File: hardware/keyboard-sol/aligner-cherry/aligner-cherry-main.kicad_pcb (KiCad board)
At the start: 2 copper layers, 324 x 116.9 mm, 75 parts, among them SW10 TAB: 1.25x, SW11 I, SW12 2, SW13 Zero, SW14 Q, SW15 O, SW16 3, SW17 Dash, SW18 W, SW19 P, SW20 4, SW21 Caret, SW22 E, SW23 AT, SW24 5, SW25 LT Bracket, SW26 R, SW27 Return: 1.5x, SW28 6, SW29 Backslash, SW30 T, SW31 Line Feed, SW32 7, SW33 RT Bracket, SW34 Y, SW35 Load, SW36 LT Ctrl, SW37 J, SW38 Upper Case: 1.5x, SW39 M, SW4 ESC: 1.75x, SW40 Shift Lock: 1.5x, SW41 K, SW42 LT Shift: 1.5x, SW43 Comma, SW44 A, SW45 L, SW46 Z, SW47 Period, SW48 S, SW49 Semicolon, SW5 8, SW50 X, SW51 Slash, SW52 D, SW53 Colon, SW54 C, SW55 RT Shift: 2x, SW56 F, SW57 DEL, SW58 V, SW59 Mode Select: 1.75x, SW6 BREAK, SW60 G, SW61 Repeat: 1.25x, SW62 B, SW63 H, SW64 RT Ctrl, SW65 N, SW66 Local, SW7 U, SW70 Up Arrow, SW74 LT Arrow, SW78 Spacebar, SW8 1, SW81 RT Arrow, SW84 Down Arrow, SW87 Home, SW88 Clear, SW9 9

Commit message: Moved mounting slots from keyboard PCB to aligners
- This allows the PCB to sink below the mounting brackets.  The aligner height can
be adjusted relative to the mounting brackets using spacers.

- changed futaba aligners to use cherry stabilizers.

- bumped rev number
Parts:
- SW55: footprint unikbd:Key_MX_Aligner -> unikbd:MX_2u_aligner
- moved REF** 5.95 mm to (256.2, 114.1)
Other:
- board size 324 x 116.9 mm -> 342.4 x 117.7 mm
- board text added: "SOL-20 Cherry MX aligner (main) Rev 1.1"
- board text removed: "SOL-20 Cherry MX aligner (Main) Rev 1.0"

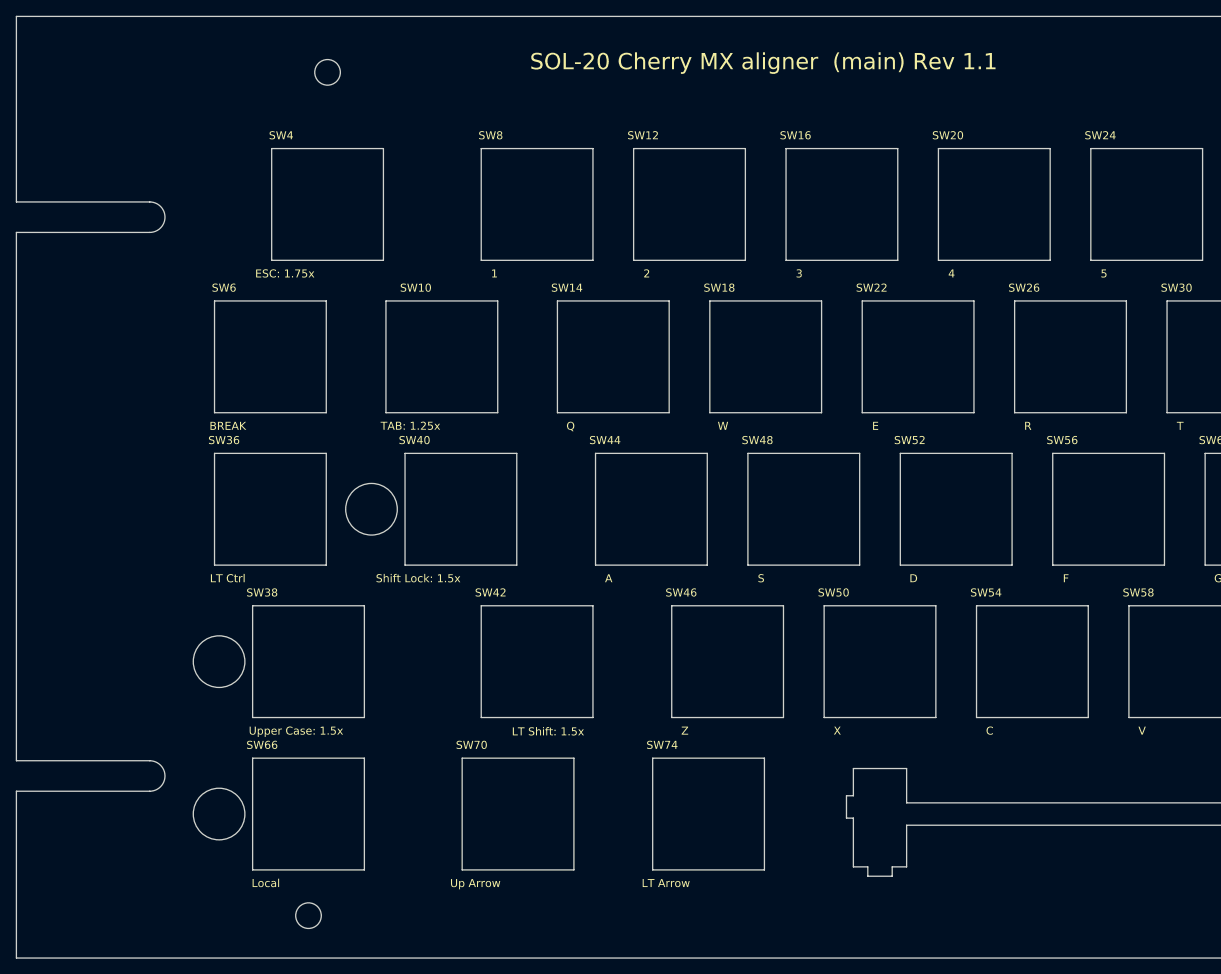
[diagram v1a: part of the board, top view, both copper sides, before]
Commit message: Adjsut mounting slots and alignment of mounting holes.
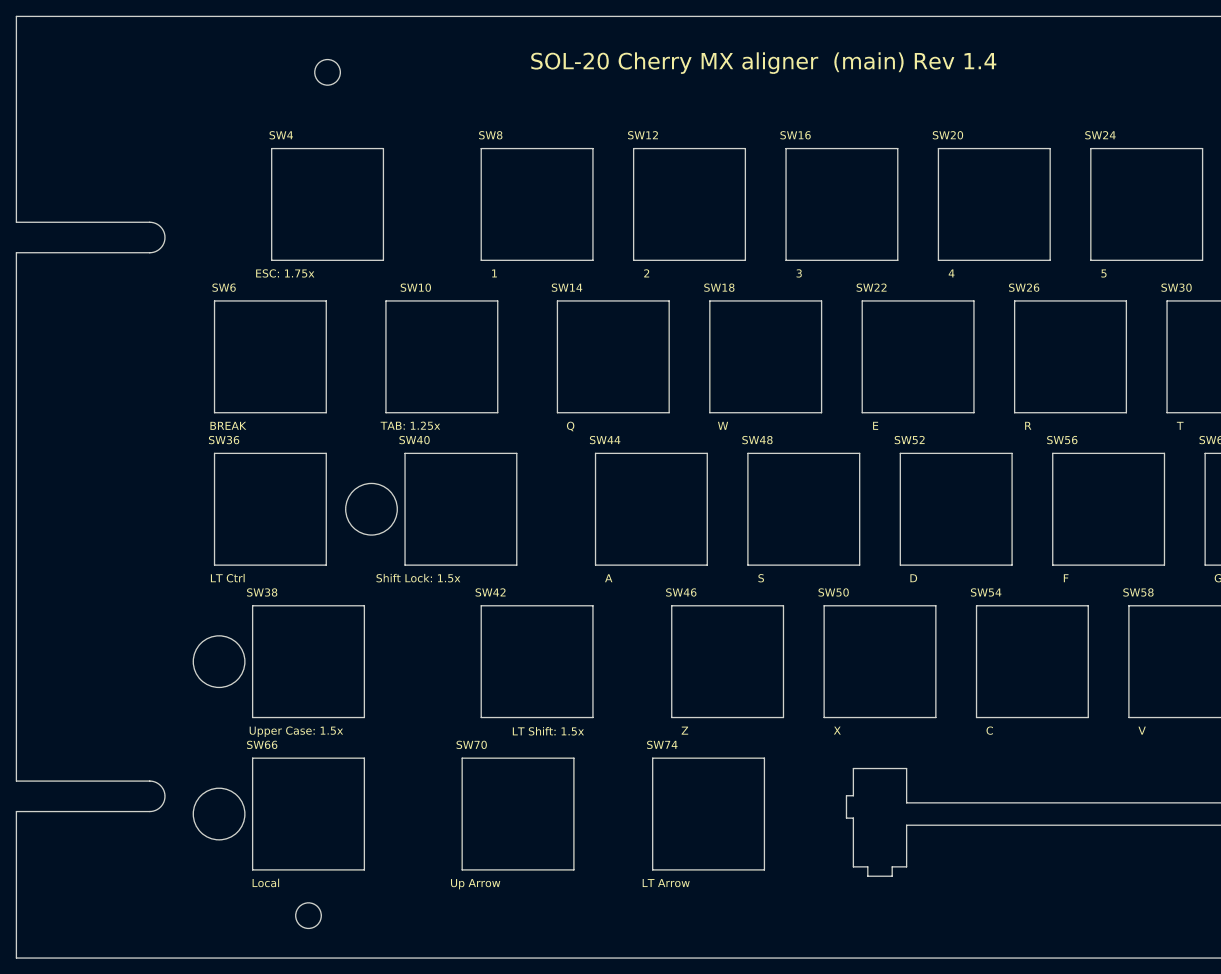
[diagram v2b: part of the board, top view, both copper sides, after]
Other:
- outline, holes or cut-outs redrawn
- board text added: "SOL-20 Cherry MX aligner (main) Rev 1.4"
- board text removed: "SOL-20 Cherry MX aligner (main) Rev 1.1"
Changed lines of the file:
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@@
   (gr_circle (center 102.16388 187.74156) (end 105.38968 187.74156) (layer Edge.Cuts) (width 0.12))
   (gr_circle (center 121.21388 168.69156) (end 124.43968 168.69156) (layer Edge.Cuts) (width 0.12))
-  (gr_text "SOL-20 Cherry MX aligner  (main) Rev 1.1\n" (at 140.9954 112.7506) (layer F.SilkS)
+  (gr_text "SOL-20 Cherry MX aligner  (main) Rev 1.4" (at 140.9954 112.7506) (layer F.SilkS)
     (effects (font (size 2.032 2.032) (thickness 0.2032)) (justify left))
   )
@@
     (effects (font (size 2.032 2.032) (thickness 0.3048)) (justify left))
   )
-  (gr_line (start 76.82738 134.08914) (end 76.82738 200.12914) (layer Edge.Cuts) (width 0.1016))
-  (gr_line (start 76.82738 107.0864) (end 76.82738 130.27914) (layer Edge.Cuts) (width 0.1016))
-  (gr_line (start 93.49613 130.27914) (end 76.82738 130.27914) (layer Edge.Cuts) (width 0.1016))
-  (gr_line (start 93.49613 134.08914) (end 76.82738 134.08914) (layer Edge.Cuts) (width 0.1016))
-  (gr_arc (start 93.49613 132.18414) (end 93.49613 130.27914) (angle 180) (layer Edge.Cuts) (width 0.1016))
-  (gr_line (start 93.49613 203.93914) (end 76.82738 203.93914) (layer Edge.Cuts) (width 0.1016))
-  (gr_line (start 93.49613 200.12914) (end 76.82738 200.12914) (layer Edge.Cuts) (width 0.1016))
-  (gr_line (start 76.82738 224.79) (end 76.82738 203.93914) (layer Edge.Cuts) (width 0.1016))
-  (gr_arc (start 93.49613 202.03414) (end 93.49613 200.12914) (angle 180) (layer Edge.Cuts) (width 0.1016))
+  (gr_line (start 76.82738 136.62914) (end 76.82738 202.66914) (layer Edge.Cuts) (width 0.1016))
+  (gr_line (start 76.82738 107.0864) (end 76.82738 132.81914) (layer Edge.Cuts) (width 0.1016))
+  (gr_line (start 93.49613 132.81914) (end 76.82738 132.81914) (layer Edge.Cuts) (width 0.1016))
+  (gr_line (start 93.49613 136.62914) (end 76.82738 136.62914) (layer Edge.Cuts) (width 0.1016))
+  (gr_arc (start 93.49613 134.72414) (end 93.49613 132.81914) (angle 180) (layer Edge.Cuts) (width 0.1016))
+  (gr_line (start 93.49613 206.47914) (end 76.82738 206.47914) (layer Edge.Cuts) (width 0.1016))
+  (gr_line (start 93.49613 202.66914) (end 76.82738 202.66914) (layer Edge.Cuts) (width 0.1016))
+  (gr_line (start 76.82738 224.79) (end 76.82738 206.47914) (layer Edge.Cuts) (width 0.1016))
+  (gr_arc (start 93.49613 204.57414) (end 93.49613 202.66914) (angle 180) (layer Edge.Cuts) (width 0.1016))
   (gr_line (start 76.82738 224.79) (end 419.227 224.79) (layer Edge.Cuts) (width 0.1))
   (gr_line (start 419.227 107.0864) (end 76.82738 107.0864) (layer Edge.Cuts) (width 0.1016))
